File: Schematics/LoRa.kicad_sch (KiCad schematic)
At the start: 2 parts, among them J6 Conn_Coaxial_Small, U3 RFM95W-915S2

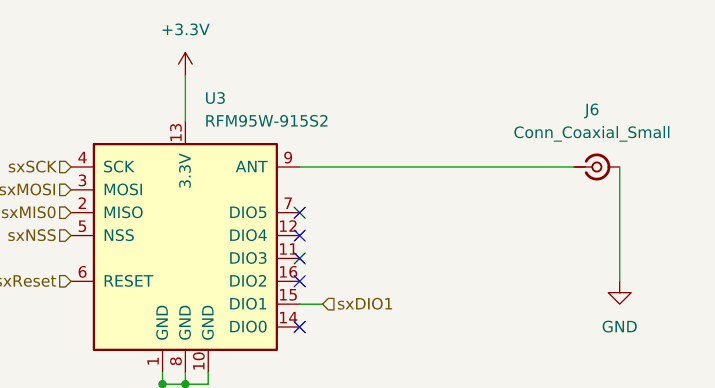
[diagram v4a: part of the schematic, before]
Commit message: added lora correct and organizing sheet pins
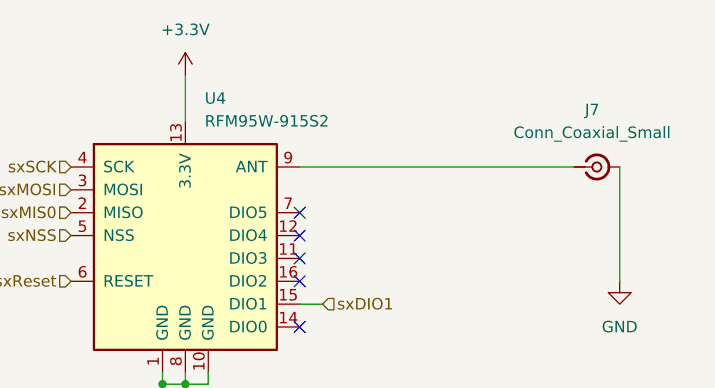
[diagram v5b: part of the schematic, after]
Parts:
- renumbered J6 to J7, U3 to U4
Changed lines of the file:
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@@
 		(dnp no)
 		(fields_autoplaced yes)
-		(property "Reference" "#PWR055"
+		(property "Reference" "#PWR058"
 			(at 128.27 109.22 0)
 			(effects
@@
 			(project ""
 				(path "/6cb3dda3-5fe8-4715-b831-354360aa3199/97ae08f8-7044-40a2-9385-378b47d6b9a1"
-					(reference "#PWR055")
+					(reference "#PWR058")
 					(unit 1)
 				)
@@
 		(dnp no)
 		(fields_autoplaced yes)
-		(property "Reference" "#PWR056"
+		(property "Reference" "#PWR059"
 			(at 130.81 69.85 0)
 			(effects
@@
 			(project ""
 				(path "/6cb3dda3-5fe8-4715-b831-354360aa3199/97ae08f8-7044-40a2-9385-378b47d6b9a1"
-					(reference "#PWR056")
+					(reference "#PWR059")
 					(unit 1)
 				)
@@
 		(dnp no)
 		(fields_autoplaced yes)
-		(property "Reference" "J6"
+		(property "Reference" "J7"
 			(at 176.0104 69.85 0)
 			(effects
@@
 			(project "flightcomputer2"
 				(path "/6cb3dda3-5fe8-4715-b831-354360aa3199/97ae08f8-7044-40a2-9385-378b47d6b9a1"
-					(reference "J6")
+					(reference "J7")
 					(unit 1)
 				)
@@
 		(dnp no)
 		(fields_autoplaced yes)
-		(property "Reference" "#PWR0104"
+		(property "Reference" "#PWR060"
 			(at 179.07 95.25 0)
 			(effects
@@
 			(project ""
 				(path "/6cb3dda3-5fe8-4715-b831-354360aa3199/97ae08f8-7044-40a2-9385-378b47d6b9a1"
-					(reference "#PWR0104")
+					(reference "#PWR060")
 					(unit 1)
 				)
@@
 		(dnp no)
 		(fields_autoplaced yes)
-		(property "Reference" "U3"
+		(property "Reference" "U4"
 			(at 132.9533 68.58 0)
 			(effects
@@
 			(project ""
 				(path "/6cb3dda3-5fe8-4715-b831-354360aa3199/97ae08f8-7044-40a2-9385-378b47d6b9a1"
-					(reference "U3")
-					(unit 1)
-				)
+					(reference "U4")
+					(unit 1)
+				)

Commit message: finished pin assignments and ran ERC all good ready for layout
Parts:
- U4: footprint (none) -> myFootprints:XCVR_RFM95W-915S2; LCSC Part (none) -> C2844473
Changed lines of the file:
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@@
+			)
+		)
+		(property "Description_1" ""
+			(at 176.53 76.2 0)
+			(effects
+				(font
+					(size 1.27 1.27)
+				)
+				(hide yes)
+			)
+		)
+		(property "MF" ""
+			(at 176.53 76.2 0)
+			(effects
+				(font
+					(size 1.27 1.27)
+				)
+				(hide yes)
+			)
+		)
+		(property "MP" ""
+			(at 176.53 76.2 0)
+			(effects
+				(font
+					(size 1.27 1.27)
+				)
+				(hide yes)
+			)
+		)
+		(property "Package" ""
+			(at 176.53 76.2 0)
+			(effects
+				(font
+					(size 1.27 1.27)
+				)
+				(hide yes)
+			)
+		)
+		(property "Price" ""
+			(at 176.53 76.2 0)
+			(effects
+				(font
+					(size 1.27 1.27)
+				)
+				(hide yes)
+			)
+		)
+		(property "Purchase-URL" ""
+			(at 176.53 76.2 0)
+			(effects
+				(font
+					(size 1.27 1.27)
+				)
+				(hide yes)
 			)
 		)
@@
 			)
 		)
-		(property "Footprint" ""
+		(property "Footprint" "myFootprints:XCVR_RFM95W-915S2"
 			(at 46.99 41.91 0)
 			(effects
@@
 			(at 130.81 83.82 0)
 			(effects
+				(font
+					(size 1.27 1.27)
+				)
+				(hide yes)
+			)
+		)
+		(property "Description_1" ""
+			(at 130.81 83.82 0)
+			(effects
+				(font
+					(size 1.27 1.27)
+				)
+				(hide yes)
+			)
+		)
+		(property "MF" ""
+			(at 130.81 83.82 0)
+			(effects
+				(font
+					(size 1.27 1.27)
+				)
+				(hide yes)
+			)
+		)
+		(property "MP" ""
+			(at 130.81 83.82 0)
+			(effects
+				(font
+					(size 1.27 1.27)
+				)
+				(hide yes)
+			)
+		)
+		(property "Package" ""
+			(at 130.81 83.82 0)
+			(effects
+				(font
+					(size 1.27 1.27)
+				)
+				(hide yes)
+			)
+		)
+		(property "Price" ""
+			(at 130.81 83.82 0)
+			(effects
+				(font
+					(size 1.27 1.27)
+				)
+				(hide yes)
+			)
+		)
+		(property "Purchase-URL" ""
+			(at 130.81 83.82 0)
+			(effects
+				(font
+					(size 1.27 1.27)
+				)
+				(hide yes)
+			)
+		)
+		(property "LCSC Part" "C2844473"
+			(at 130.81 83.82 0)
+			(effects

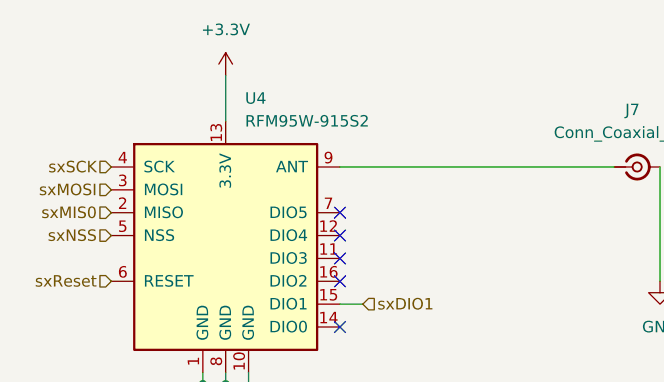
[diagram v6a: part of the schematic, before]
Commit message: first layout need to go over schematic
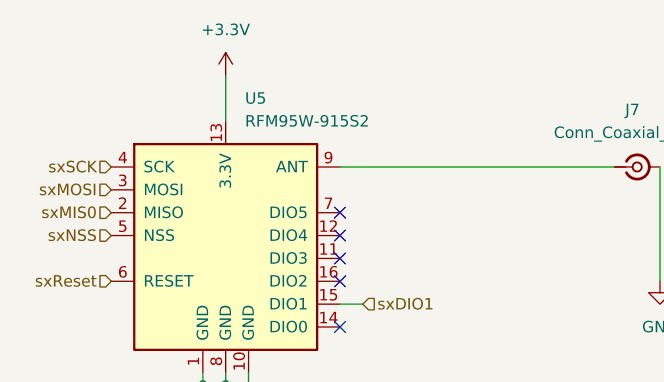
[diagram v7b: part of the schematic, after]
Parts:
- renumbered U4 to U5
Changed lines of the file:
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@@
 		(dnp no)
 		(fields_autoplaced yes)
-		(property "Reference" "#PWR058"
+		(property "Reference" "#PWR064"
 			(at 128.27 109.22 0)
 			(effects
@@
 			(project ""
 				(path "/6cb3dda3-5fe8-4715-b831-354360aa3199/97ae08f8-7044-40a2-9385-378b47d6b9a1"
-					(reference "#PWR058")
+					(reference "#PWR064")
 					(unit 1)
 				)
@@
 		(dnp no)
 		(fields_autoplaced yes)
-		(property "Reference" "#PWR059"
+		(property "Reference" "#PWR065"
 			(at 130.81 69.85 0)
 			(effects
@@
 			(project ""
 				(path "/6cb3dda3-5fe8-4715-b831-354360aa3199/97ae08f8-7044-40a2-9385-378b47d6b9a1"
-					(reference "#PWR059")
+					(reference "#PWR065")
 					(unit 1)
 				)
@@
 		(dnp no)
 		(fields_autoplaced yes)
-		(property "Reference" "#PWR060"
+		(property "Reference" "#PWR066"
 			(at 179.07 95.25 0)
 			(effects
@@
 			(project ""
 				(path "/6cb3dda3-5fe8-4715-b831-354360aa3199/97ae08f8-7044-40a2-9385-378b47d6b9a1"
-					(reference "#PWR060")
+					(reference "#PWR066")
 					(unit 1)
 				)
@@
 		(dnp no)
 		(fields_autoplaced yes)
-		(property "Reference" "U4"
+		(property "Reference" "U5"
 			(at 132.9533 68.58 0)
 			(effects
@@
 			(project ""
 				(path "/6cb3dda3-5fe8-4715-b831-354360aa3199/97ae08f8-7044-40a2-9385-378b47d6b9a1"
-					(reference "U4")
+					(reference "U5")
 					(unit 1)
 				)
